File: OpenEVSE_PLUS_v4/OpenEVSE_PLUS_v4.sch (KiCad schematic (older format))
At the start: 76 parts, among them IC1 MID400, IC2 ATMEGA328P-AU, IC3 LM358, IC4 LF353, IC5 AQH1213, IC6 MID400, Q1 16000, Q2 2222A, Q3 2222A

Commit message: removed non EU related parts
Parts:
- removed AC_LINE1, AC_RELAY1, AC_TEST1: TE 1776275-2, OpenEVSE_PLUS_v4:SCREWTERMINAL-3.5MM-2_LOCK, symbol OpenEVSE_PLUS_v4-eagle-import:M023.5MM_LOCK
- removed D8: 1N4004, OpenEVSE_PLUS_v4:SMA, symbol OpenEVSE_PLUS_v4-eagle-import:MBRA340T3
- removed F1, F2: BEL1AFUSE, OpenEVSE_PLUS_v4:BELFUSE1A, symbol OpenEVSE_PLUS_v4-eagle-import:BEL1AFUSE
- removed IC6: MID400, OpenEVSE_PLUS_v4:DIP08, symbol OpenEVSE_PLUS_v4-eagle-import:MID400
- removed R22: 47K, OpenEVSE_PLUS_v4:AXIAL-0.4, symbol OpenEVSE_PLUS_v4-eagle-import:RESISTORPTH-1_4W
- removed U$1: MPM-04E-1205, OpenEVSE_PLUS_v4:MPM-04E-1205, symbol OpenEVSE_PLUS_v4-eagle-import:MPM-04E-1205
- added RELAY2: AC, OpenEVSE_PLUS_v4:SCREWTERMINAL-3.5MM-3_LOCK.007S, symbol OpenEVSE_PLUS_v4-eagle-import:M03SCREW_LOCK
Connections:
- net labels added: AC-N1, AC-N2, ACTST, BTN1
- net labels removed: ACRELAY, AC_TEST, FUSEL, FUSEN
- wire segments 242 -> 226
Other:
- moved on the sheet: D7, R29, R4

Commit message: updated footprints to kicad
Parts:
- removed R4: 47K, OpenEVSE_PLUS_v4:AXIAL-0.4, symbol OpenEVSE_PLUS_v4-eagle-import:RESISTORPTH-1_4W
- added H1, H2: MountingHole_Pad, MountingHole:MountingHole_2.2mm_M2_DIN965_Pad, symbol Mechanical:MountingHole_Pad
- added H3, H4: MountingHole, MountingHole:MountingHole_2.2mm_M2, symbol Mechanical:MountingHole
- added R4: 56k 1W, Resistor_THT:R_Axial_DIN0207_L6.3mm_D2.5mm_P10.16mm_Horizontal, symbol Device:R_US
- .1: footprint OpenEVSE_PLUS_v4:1X06_LOCK -> Connector_PinHeader_2.54mm:PinHeader_1x06_P2.54mm_Vertical
- A_CT1: footprint OpenEVSE_PLUS_v4:1X02 -> Connector_PinHeader_2.54mm:PinHeader_1x02_P2.54mm_Vertical
- C1, C10, C11, C12, C13, C2, C3, C5, C6, C7, C8, C9: footprint OpenEVSE_PLUS_v4:0805 -> Capacitor_SMD:C_0805_2012Metric
- C14, C4: footprint OpenEVSE_PLUS_v4:EIA3216 -> Capacitor_SMD:C_1206_3216Metric
- D1, Q2, Q3: footprint OpenEVSE_PLUS_v4:SOT23 -> Package_TO_SOT_SMD:SOT-23
- D2, D3, D4, D5, D6: footprint OpenEVSE_PLUS_v4:SOD123 -> Diode_SMD:D_1206_3216Metric
- D7: footprint OpenEVSE_PLUS_v4:SMA -> Diode_SMD:D_SMA
- DCDC1: value MD112D-12E -> AIMTEC; footprint OpenEVSE_PLUS_v4:DCDC_SIP -> Converter_DCDC:Converter_DCDC_muRata_NMAxxxxSC_THT; symbol OpenEVSE_PLUS_v4-eagle-import:DCDC_SIP -> Regulator_Switching:TMR_1-1222
- G_CT1, I2C1: footprint OpenEVSE_PLUS_v4:1X04_LOCK -> Connector_PinHeader_2.54mm:PinHeader_1x04_P2.54mm_Vertical
- IC1: footprint OpenEVSE_PLUS_v4:DIP08 -> Package_DIP:DIP-8_W7.62mm
- IC2: footprint OpenEVSE_PLUS_v4:TQFP32-08 -> Package_QFP:TQFP-32_7x7mm_P0.8mm
- IC3, IC4: footprint OpenEVSE_PLUS_v4:SO08 -> Package_SO:SOIC-8_3.9x4.9mm_P1.27mm
- IC5: footprint OpenEVSE_PLUS_v4:DIP7 -> Package_DIP:DIP-8-N7_W7.62mm
- ISP1: footprint OpenEVSE_PLUS_v4:AVRISP -> Connector_PinHeader_2.54mm:PinHeader_2x03_P2.54mm_Vertical
- Q1: footprint OpenEVSE_PLUS_v4:NX3225 -> Crystal:Crystal_SMD_EuroQuartz_MT-4Pin_3.2x2.5mm
- R1, R10, R11, R12, R13, R14, R15, R16, R17, R18, R19, R2, R20, R21, R23, R24, R25, R26, R29, R3, R5, R6, R7, R8, R9: footprint OpenEVSE_PLUS_v4:0805 -> Resistor_SMD:R_0805_2012Metric
- R27, R28: footprint OpenEVSE_PLUS_v4:R1206 -> Resistor_SMD:R_1206_3216Metric
- RELAY1, RELAY2: footprint OpenEVSE_PLUS_v4:SCREWTERMINAL-3.5MM-3_LOCK.007S -> TerminalBlock_Phoenix:TerminalBlock_Phoenix_PT-1,5-3-3.5-H_1x03_P3.50mm_Horizontal
- TVS1: footprint OpenEVSE_PLUS_v4:SMB -> Diode_SMD:D_SMB
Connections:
- wire segments 226 -> 229

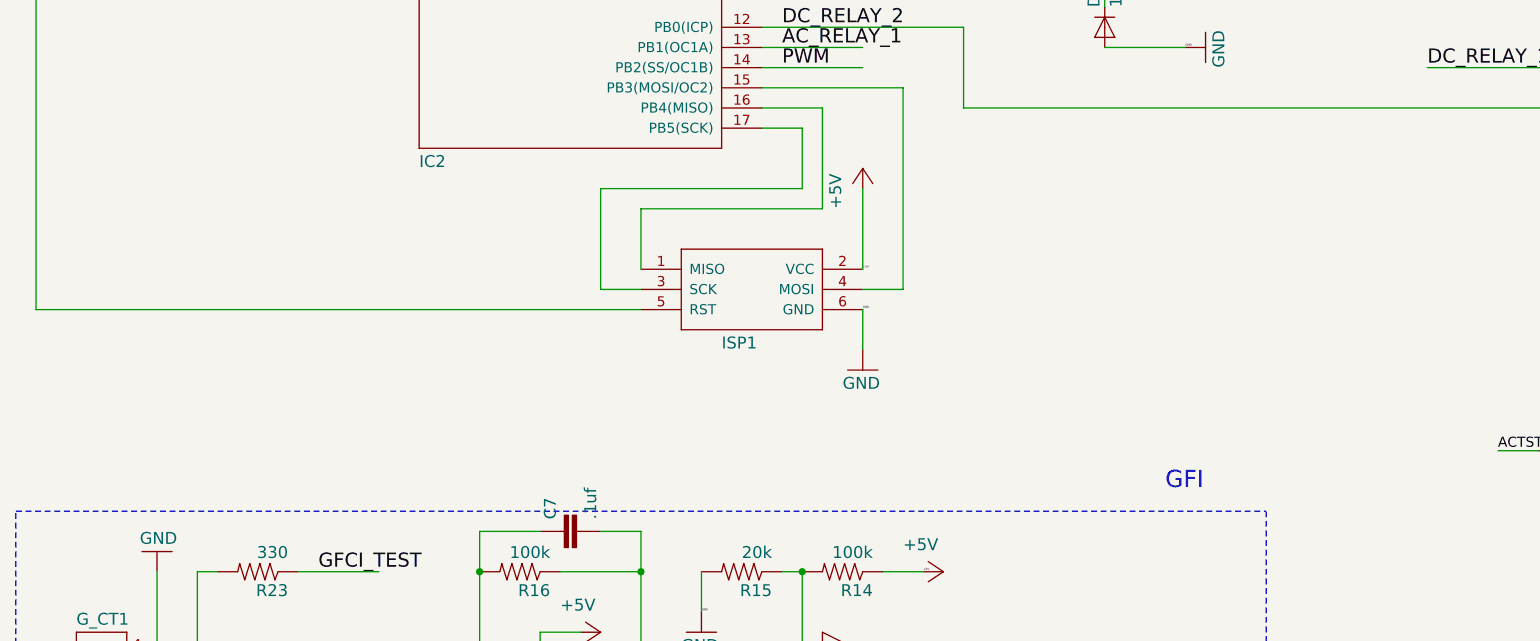
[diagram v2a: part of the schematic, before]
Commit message: added 3.3 and 5v regulators
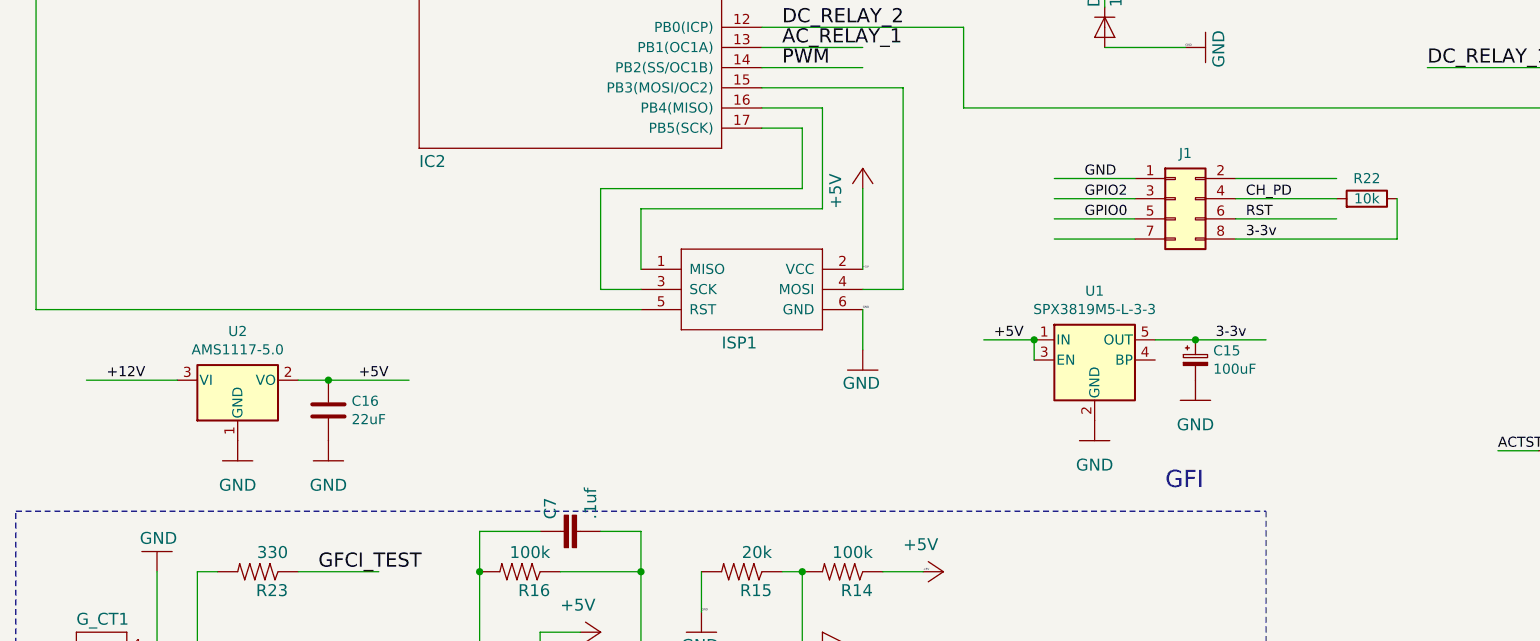
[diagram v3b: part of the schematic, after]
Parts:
- added C15: 100uF, Capacitor_THT:CP_Radial_D5.0mm_P2.50mm, symbol Device:CP_Small
- added C16: 22uF, Capacitor_SMD:C_1206_3216Metric, symbol Device:C
- added J1: Conn_02x04_Odd_Even, Connector_PinSocket_2.54mm:PinSocket_2x04_P2.54mm_Vertical, symbol Connector_Generic:Conn_02x04_Odd_Even
- added R22: 10k, Resistor_SMD:R_0805_2012Metric, symbol Device:R
- added U1: SPX3819M5-L-3-3, Package_TO_SOT_SMD:SOT-23-5, symbol Regulator_Linear:SPX3819M5-L-3-3
- added U2: AMS1117-5.0, Package_TO_SOT_SMD:SOT-223-3_TabPin2, symbol Regulator_Linear:AMS1117-5.0
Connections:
- net labels added: 3-3v, CH_PD, GPIO0, GPIO2, RST
- wire segments 229 -> 245
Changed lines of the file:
@@
 	0    1    1    0
 $EndComp
+$Comp
+L Connector_Generic:Conn_02x04_Odd_Even J1
+U 1 1 5E9C1292
+P 6950 6050
+F 0 "J1" H 7000 6275 50  0000 C CNN
+F 1 "Conn_02x04_Odd_Even" H 7000 6276 50  0001 C CNN
+F 2 "Connector_PinSocket_2.54mm:PinSocket_2x04_P2.54mm_Vertical" H 6950 6050 50  0001 C CNN
+F 3 "~" H 6950 6050 50  0001 C CNN
+	1    6950 6050
+	1    0    0    -1
+$EndComp
+Wire Wire Line
+	6750 5950 6350 5950
+Wire Wire Line
+	6750 6050 6350 6050
+Wire Wire Line
+	6750 6150 6350 6150
+Wire Wire Line
+	6750 6250 6350 6250
+Wire Wire Line
+	7250 6150 7750 6150
+Wire Wire Line
+	7250 6050 7750 6050
+Wire Wire Line
+	7250 5950 7750 5950
+Text Label 6500 5950 0    50   ~ 0
+GND
+Text Label 6500 6050 0    50   ~ 0
+GPIO2
+Text Label 6500 6150 0    50   ~ 0
+GPIO0
+Text Label 7300 6250 0    50   ~ 0
+3-3v
+Text Label 7300 6150 0    50   ~ 0
+RST
+Text Label 7300 6050 0    50   ~ 0
+CH_PD
+$Comp
+L Device:R R22
+U 1 1 5EA427A3
+P 7900 6050
+F 0 "R22" V 8000 6050 50  0000 C CNN
+F 1 "10k" V 7900 6050 50  0000 C CNN
+F 2 "Resistor_SMD:R_0805_2012Metric" V 7830 6050 50  0001 C CNN
+F 3 "~" H 7900 6050 50  0001 C CNN
+	1    7900 6050
+	0    1    -1   0
+$EndComp
+Wire Wire Line
+	8050 6050 8050 6250
+Wire Wire Line
+	7250 6250 8050 6250
+$Comp
+L Regulator_Linear:SPX3819M5-L-3-3 U1
+U 1 1 5EA6F4AB
+P 6550 6850
+F 0 "U1" H 6550 7192 50  0000 C CNN
+F 1 "SPX3819M5-L-3-3" H 6550 7101 50  0000 C CNN
+F 2 "Package_TO_SOT_SMD:SOT-23-5" H 6550 7175 50  0001 C CNN
+F 3 "https://www.exar.com/content/document.ashx?id=22106&languageid=1033&type=Datasheet&partnumber=SPX3819&filename=SPX3819.pdf&part=SPX3819" H 6550 6850 50  0001 C CNN
+	1    6550 6850
+	1    0    0    -1
+$EndComp
+$Comp
+L OpenEVSE_PLUS_v4-eagle-import:GND #GND02
+U 1 1 5EAA932D
+P 6550 7250
+F 0 "#GND02" H 6550 7250 50  0001 C CNN
+F 1 "GND" H 6550 7129 59  0000 C CNN
+F 2 "" H 6550 7250 50  0001 C CNN
+F 3 "" H 6550 7250 50  0001 C CNN
+	1    6550 7250
+	1    0    0    -1
+$EndComp
+Wire Wire Line
+	6250 6750 6250 6850
+Wire Wire Line
+	6250 6750 6000 6750
+Connection ~ 6250 6750
+Text Label 6050 6750 0    50   ~ 0
++5V
+Wire Wire Line
+	6850 6750 7050 6750
+$Comp
+L Device:CP_Small C15
+U 1 1 5EADECF9
+P 7050 6850
+F 0 "C15" H 7138 6896 50  0000 L CNN
+F 1 "100uF" H 7138 6805 50  0000 L CNN
+F 2 "Capacitor_THT:CP_Radial_D5.0mm_P2.50mm" H 7050 6850 50  0001 C CNN
+F 3 "~" H 7050 6850 50  0001 C CNN
+	1    7050 6850
+	1    0    0    -1
+$EndComp
+Connection ~ 7050 6750
+Wire Wire Line
+	7050 6750 7400 6750
+$Comp
+L OpenEVSE_PLUS_v4-eagle-import:GND #GND018
+U 1 1 5EADF2EA
+P 7050 7050
+F 0 "#GND018" H 7050 7050 50  0001 C CNN
+F 1 "GND" H 7050 6929 59  0000 C CNN
+F 2 "" H 7050 7050 50  0001 C CNN
+F 3 "" H 7050 7050 50  0001 C CNN
+	1    7050 7050
+	1    0    0    -1
+$EndComp
+Text Label 7150 6750 0    50   ~ 0
+3-3v
+$Comp
+L Regulator_Linear:AMS1117-5.0 U2
+U 1 1 5EAECFA7
+P 2300 6950
+F 0 "U2" H 2300 7192 50  0000 C CNN
+F 1 "AMS1117-5.0" H 2300 7101 50  0000 C CNN
+F 2 "Package_TO_SOT_SMD:SOT-223-3_TabPin2" H 2300 7150 50  0001 C CNN
+F 3 "http://www.advanced-monolithic.com/pdf/ds1117.pdf" H 2400 6700 50  0001 C CNN
+	1    2300 6950
+	1    0    0    -1
+$EndComp
+Wire Wire Line
+	2000 6950 1550 6950
+Wire Wire Line
+	2600 6950 2750 6950
+$Comp
+L Device:C C16
+U 1 1 5EB1013C
+P 2750 7100
+F 0 "C16" H 2865 7146 50  0000 L CNN
+F 1 "22uF" H 2865 7055 50  0000 L CNN
+F 2 "Capacitor_SMD:C_1206_3216Metric" H 2788 6950 50  0001 C CNN
+F 3 "~" H 2750 7100 50  0001 C CNN
+	1    2750 7100
+	1    0    0    -1
+$EndComp
+Connection ~ 2750 6950
+Wire Wire Line
+	2750 6950 3150 6950
+$Comp
+L OpenEVSE_PLUS_v4-eagle-import:GND #GND030
+U 1 1 5EB10B21
+P 2750 7350
+F 0 "#GND030" H 2750 7350 50  0001 C CNN
+F 1 "GND" H 2750 7229 59  0000 C CNN
+F 2 "" H 2750 7350 50  0001 C CNN
+F 3 "" H 2750 7350 50  0001 C CNN
+	1    2750 7350
+	1    0    0    -1
+$EndComp
+$Comp
+L OpenEVSE_PLUS_v4-eagle-import:GND #GND020
+U 1 1 5EB11263
+P 2300 7350
+F 0 "#GND020" H 2300 7350 50  0001 C CNN
+F 1 "GND" H 2300 7229 59  0000 C CNN
+F 2 "" H 2300 7350 50  0001 C CNN
+F 3 "" H 2300 7350 50  0001 C CNN
+	1    2300 7350
+	1    0    0    -1
+$EndComp
+Text Label 1650 6950 0    50   ~ 0
++12V
+Text Label 2900 6950 0    50   ~ 0
++5V
 $EndSCHEMATC
